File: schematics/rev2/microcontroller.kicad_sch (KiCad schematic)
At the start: 8 parts, among them SW47 RESET, U2 ATMEGA32U4-AU, Y1 16Mhz

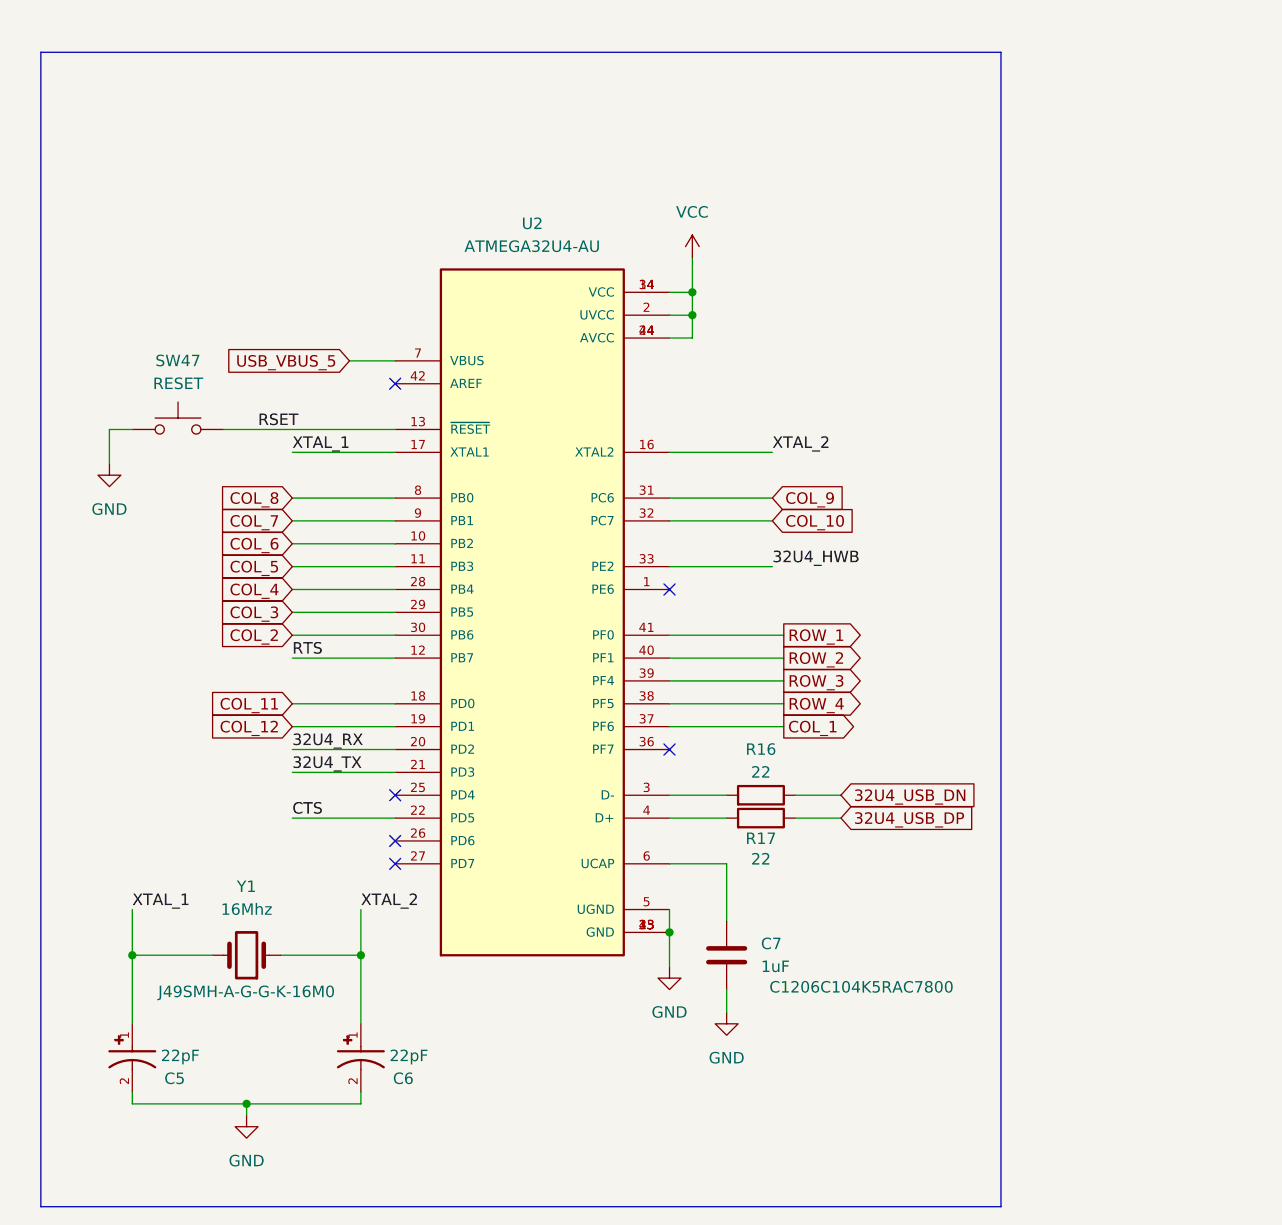
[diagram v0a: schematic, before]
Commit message: Update key layout, increase debounce, PCB update
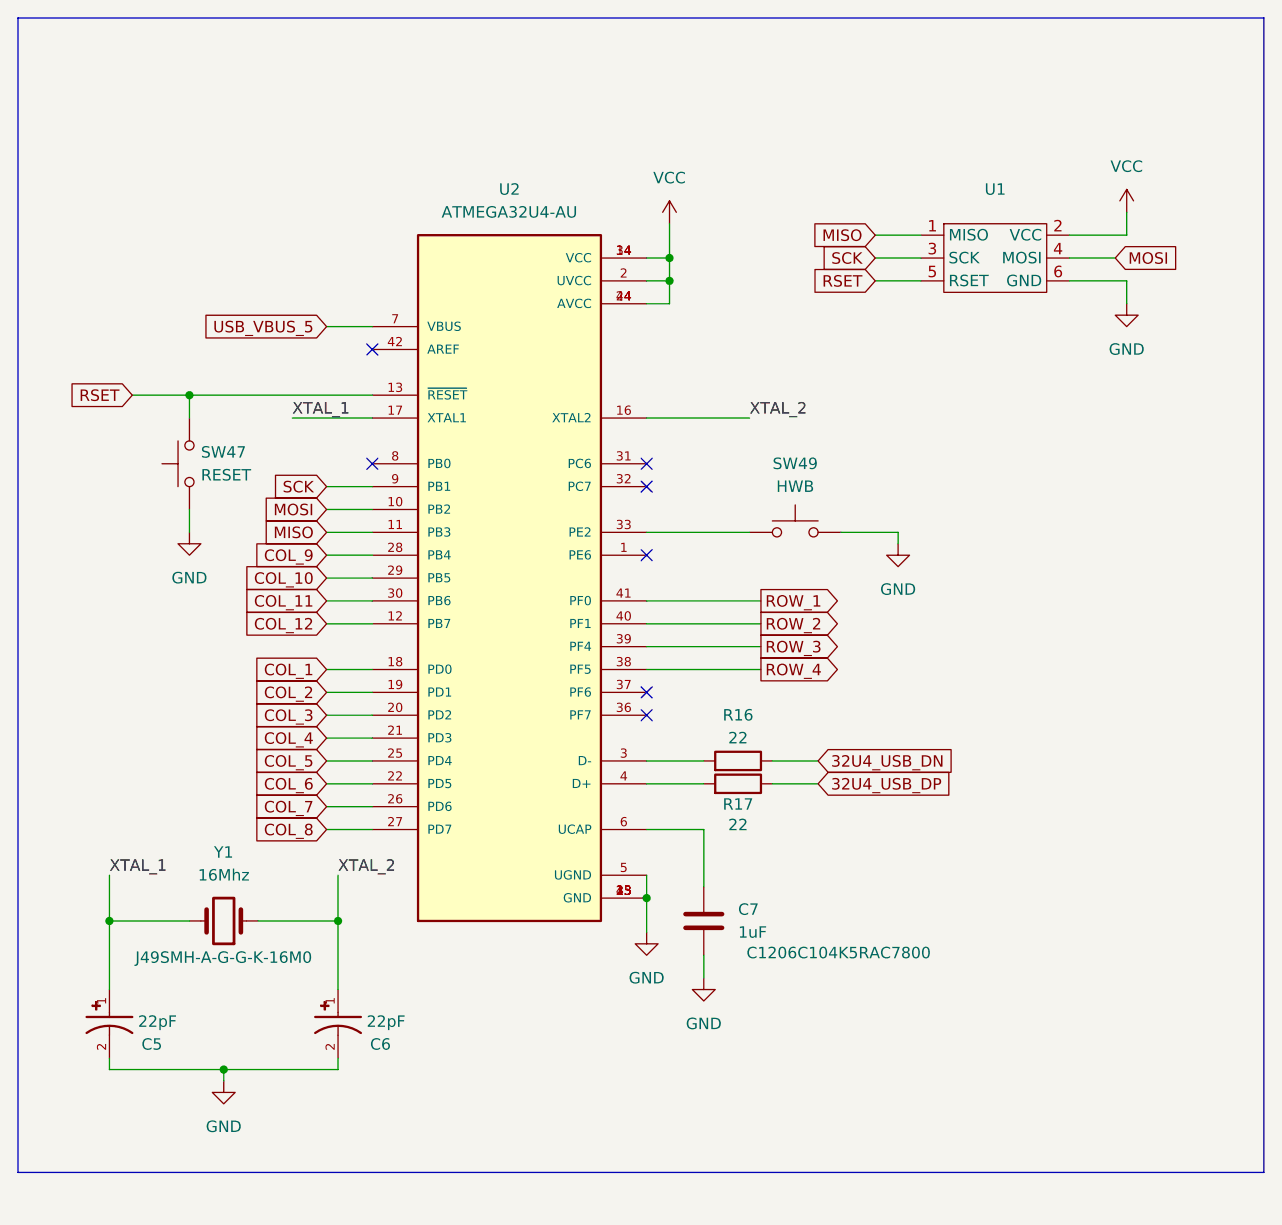
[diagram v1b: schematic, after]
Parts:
- added SW49: HWB, Jumper:SolderJumper-2_P1.3mm_Open_Pad1.0x1.5mm, symbol Switches:SW_Push
- added U1: ~, Connector_PinHeader_2.54mm:PinHeader_2x03_P2.54mm_Vertical, symbol My Parts:ICSP_Header
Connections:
- net 32U4_RX is gone; now on net COL_3: U2.20 (PD2)
- net 32U4_TX is gone; now on net COL_4: U2.21 (PD3)
- net CTS is gone; now on net COL_6: U2.22 (PD5)
- net RTS is gone; now on net COL_12: U2.12 (PB7)
- net COL_1: now also U2.18 (PD0); no longer U2.37 (PF6)
- net COL_10: now also U2.29 (PB5); no longer U2.32 (PC7)
- net COL_11: now also U2.30 (PB6); no longer U2.18 (PD0)
- net COL_12: no longer U2.19 (PD1)
- net COL_2: now also U2.19 (PD1); no longer U2.30 (PB6)
- net COL_3: no longer U2.29 (PB5)
- net COL_4: no longer U2.28 (PB4)
- net COL_5: now also U2.25 (PD4); no longer U2.11 (PB3)
- net COL_6: no longer U2.10 (PB2)
- net COL_7: now also U2.26 (PD6); no longer U2.9 (PB1)
- net COL_8: now also U2.27 (PD7); no longer U2.8 (PB0)
- net COL_9: now also U2.28 (PB4); no longer U2.31 (PC6)
- net GND: now also SW49.2, U1.6 (GND)
- net RSET: now also U1.5 (RSET)
- net VCC: now also U1.2 (VCC)
- net 32U4_HWB: no longer names the net of U2.33 (PE2)
- net 32U4_HWB: now also SW49.1
- new net MISO: U1.1 (MISO), U2.11 (PB3)
- new net MOSI: U1.4 (MOSI), U2.10 (PB2)
- new net SCK: U1.3 (SCK), U2.9 (PB1)
- no-connect marks 6 -> 7
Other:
- moved on the sheet: C5, C6, C7, R16, R17, U2, Y1

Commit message: Update schematic and board layout
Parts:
- C5, C6: Part # (none) -> C1206C220K3HAC7800
- C7: MFG # C1206C104K5RAC7800 -> (none); Part # (none) -> C1206C104K5RAC7800
- R16, R17: Part # (none) -> RMCF1206JT22R0
- U1: Part # (none) -> PH2-06-UA
- renumbered SW47 to J3, SW49 to J4
